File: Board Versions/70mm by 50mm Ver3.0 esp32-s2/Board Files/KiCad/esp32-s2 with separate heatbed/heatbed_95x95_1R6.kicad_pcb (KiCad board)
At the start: 2 copper layers, 99.1 x 77.6 mm, 5 parts

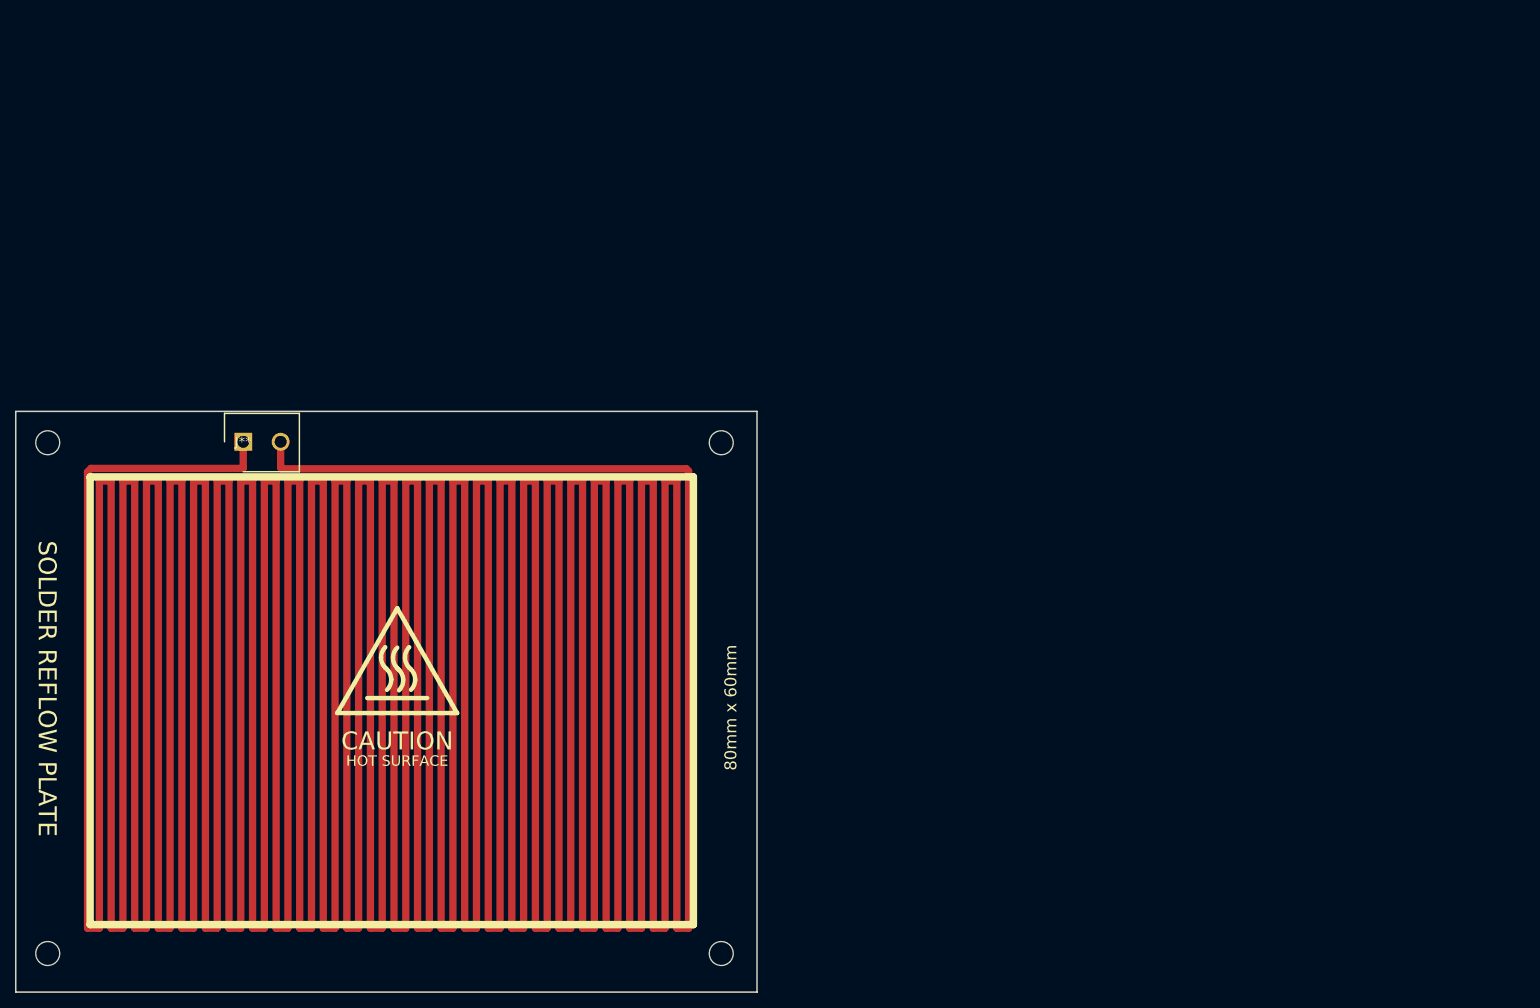
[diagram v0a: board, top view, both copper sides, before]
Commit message: Route 95x95mm board
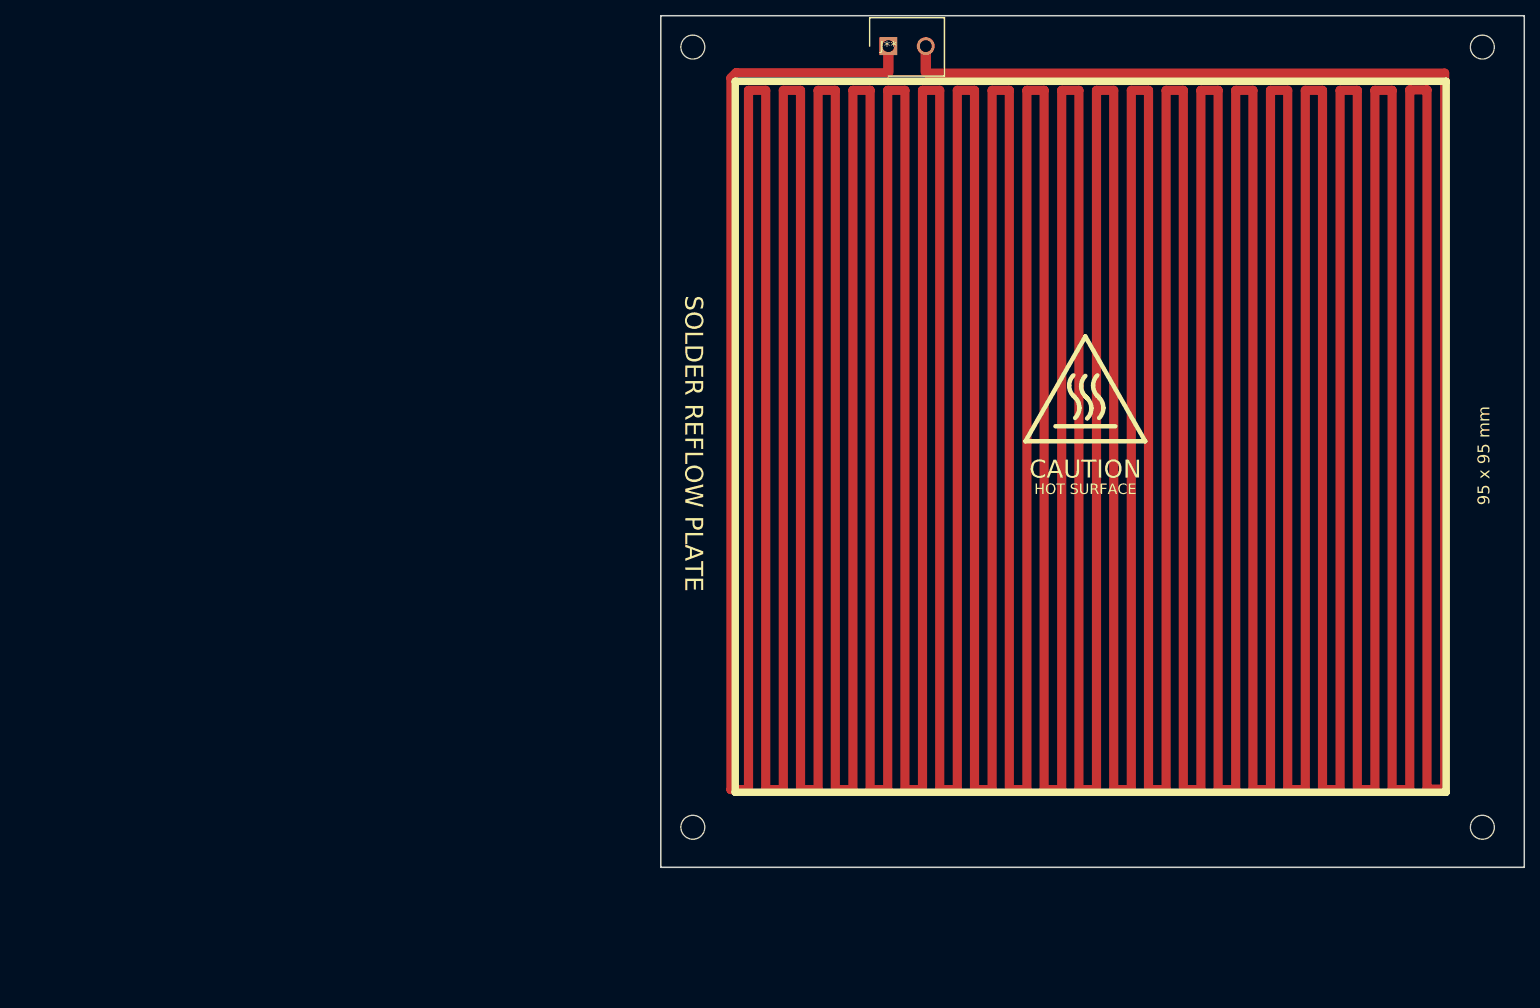
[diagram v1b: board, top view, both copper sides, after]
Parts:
- moved ? 101.1 mm to (178.1, 89.9)
- moved ? 101.1 mm to (98.1, 37.7)
- moved ? 101.1 mm to (178.1, 37.7)
- moved ? 101.1 mm to (98.1, 89.9)
- moved J** 101.1 mm to (124.2, 37.6)
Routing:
- net heater: track 3273.4 -> 4121.6 mm
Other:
- board size 99.1 x 77.6 mm -> 115.4 x 113.8 mm
- board text added: "95 x 95 mm"
- board text added: "Calculated: 1.6R@20°C"
- board text removed: "80mm x 60mm"
- board text removed: "Calculated: 1.59R@20°C"
